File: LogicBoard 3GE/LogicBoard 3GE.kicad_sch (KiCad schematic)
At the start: 162 parts, among them IC201 2363, IC202 74LS00, IC203 74LS32, IC204 2114, IC205 2114, IC206 68A09, IC207 6522, IC208 AY3-8912, IC301 MC1408, IC302 CD4052B, IC303 LF347, IC304 LF353, IC305 4066, J201 CART, J202 DB9_Male, J203 DB9_Male, J204 Power, J301 Video, J302 Audio, Q301 2N3906, Q302 2N3906, Q303 2N3904, SW201 Reset, Y201 6MHz

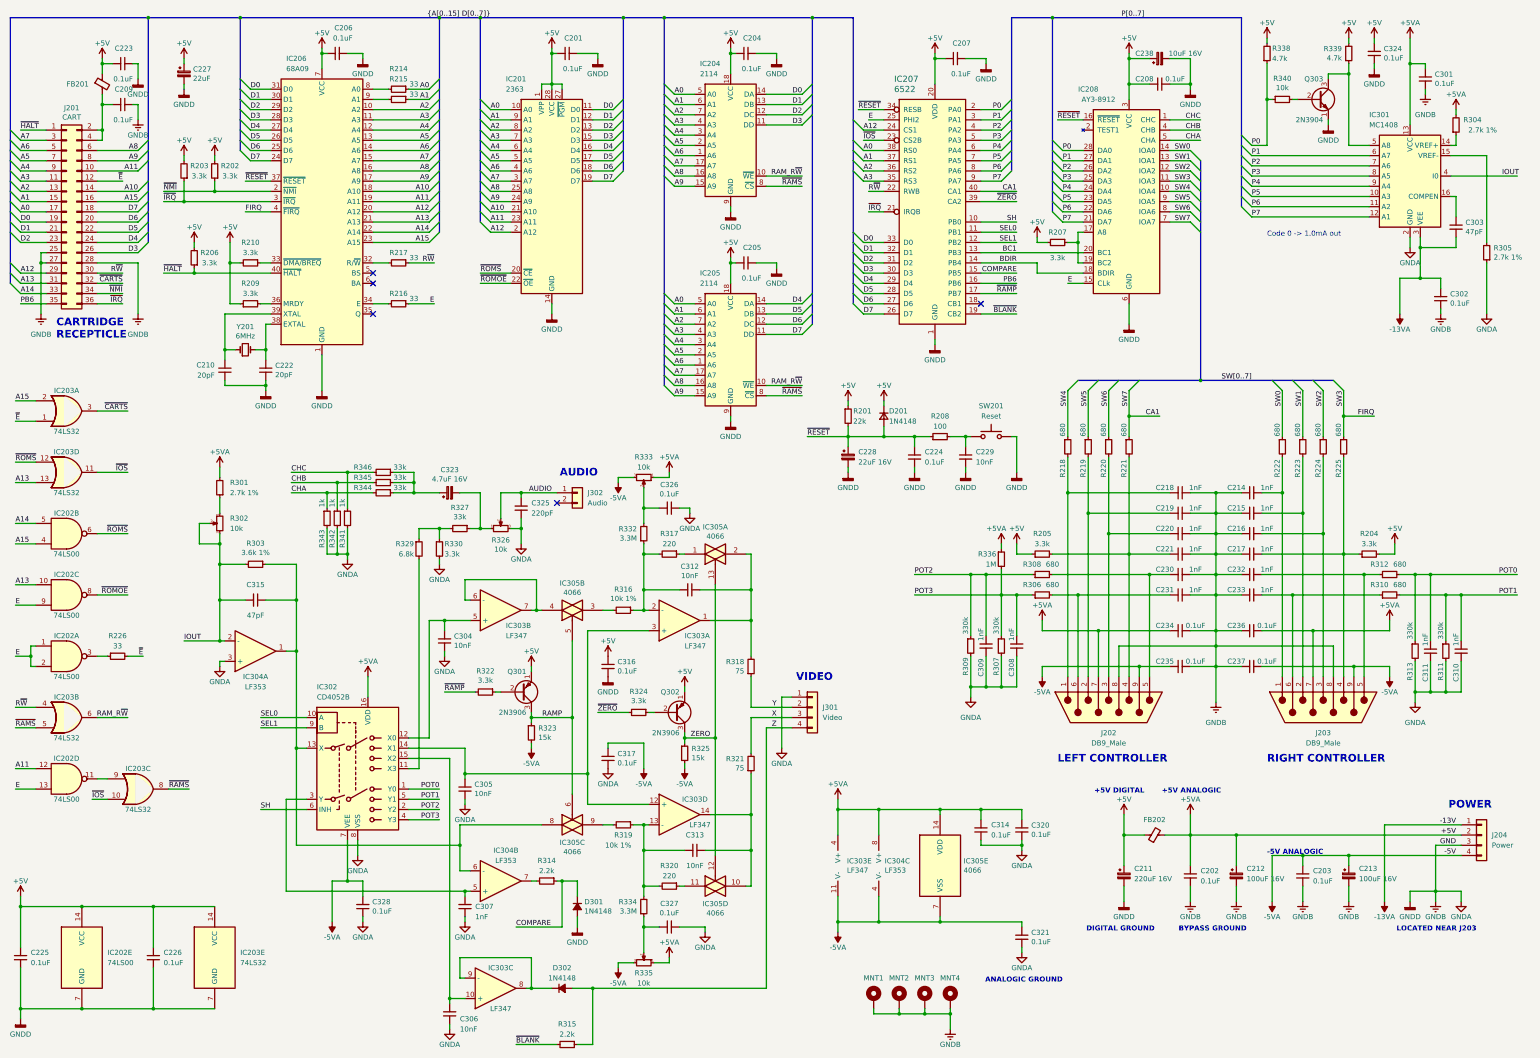
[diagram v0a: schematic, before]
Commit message: Correct inversion on IC301 bus
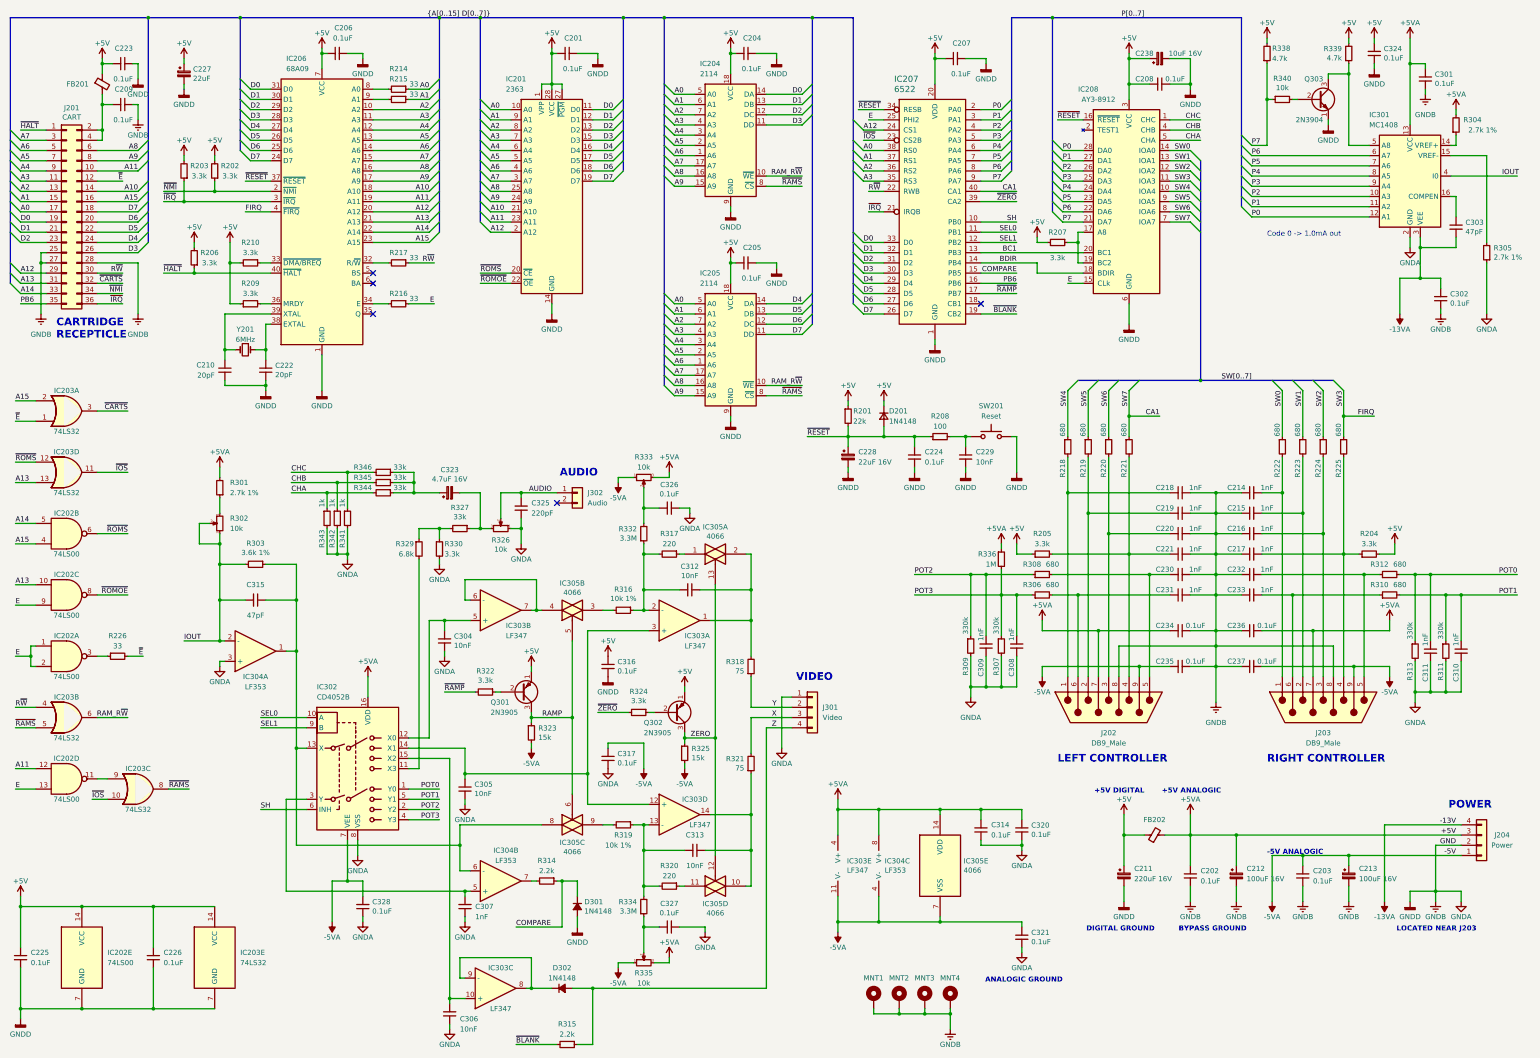
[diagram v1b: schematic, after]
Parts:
- removed Q301: 2N3906, Package_TO_SOT_THT:TO-92L_Wide, symbol Transistor_BJT:2N3906
- removed Q302: 2N3906, Package_TO_SOT_THT:TO-92_Wide, symbol Transistor_BJT:2N3906
- added Q301, Q302: 2N3905, Package_TO_SOT_THT:TO-92_Wide, symbol Transistor_BJT:2N3905
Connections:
- net +5V: now also J204.3 (Pin_3), R333.3, R335.3, Q301.1 (E), Q302.1 (E); no longer J204.2 (Pin_2), R333.1, R335.1
- net -12VA: now also J204.4 (Pin_4); no longer J204.1 (Pin_1)
- net -5VA: now also J204.1 (Pin_1), R333.1, R335.1; no longer J204.4 (Pin_4), R333.3, R335.3
- net GNDA: now also J204.2 (Pin_2), R326.1; no longer J204.3 (Pin_3), R326.3
- net P0: now also IC301.12 (A1); no longer R338.1, R340.1
- net P1: now also IC301.11 (A2); no longer IC301.6 (A7)
- net P2: now also IC301.10 (A3); no longer IC301.7 (A6)
- net P3: now also IC301.9 (A4); no longer IC301.8 (A5)
- net P4: now also IC301.8 (A5); no longer IC301.9 (A4)
- net P5: now also IC301.7 (A6); no longer IC301.10 (A3)
- net P6: now also IC301.6 (A7); no longer IC301.11 (A2)
- net P7: now also R338.1, R340.1; no longer IC301.12 (A1)
- net RAMP: now also Q301.3 (C)
- net ZERO: now also Q302.3 (C)
- net at R324.1: now also Q302.2 (B)
- net at C210.1, IC206.39 (XTAL): now also Y201.2; no longer Y201.1
- net at C222.1, IC206.38 (EXTAL): now also Y201.1; no longer Y201.2
- net at C323.2, R327.1: now also R326.3; no longer R326.1
- net at R322.1: now also Q301.2 (B)
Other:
- moved on the sheet: R326, R333, R335, Y201

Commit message: Add invisble label for BoardView
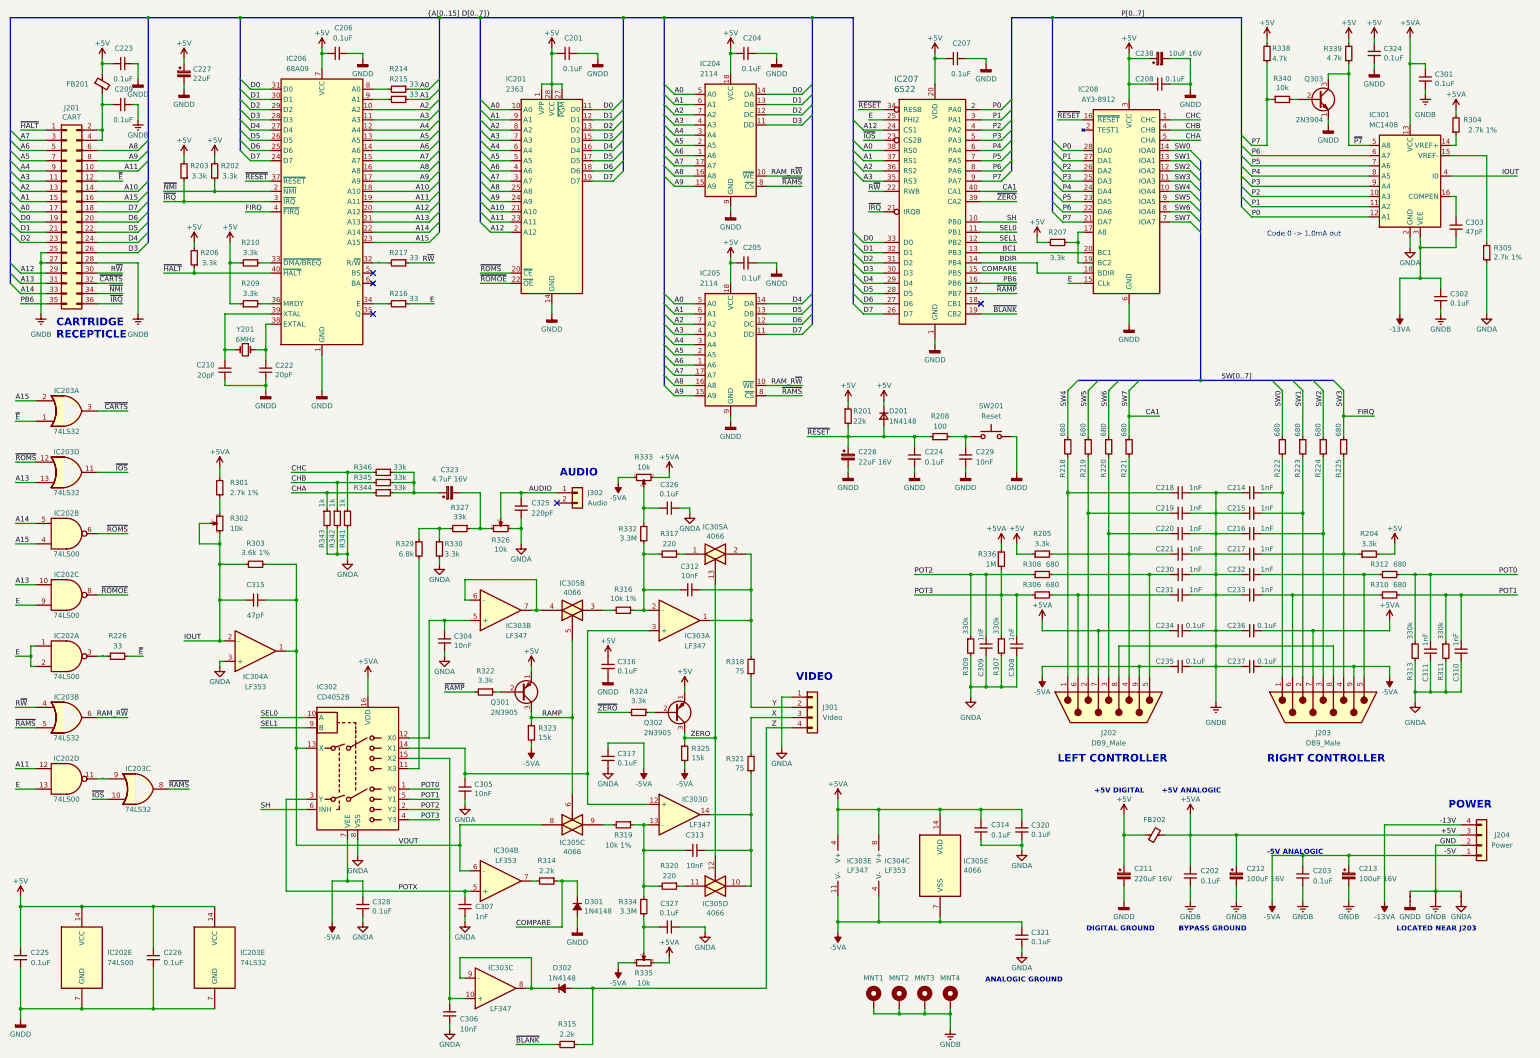
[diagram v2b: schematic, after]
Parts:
- added W1, W2, W3: W, symbol Vectrex LogicBoard:W
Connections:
- net GNDA: now also W3.1; no longer C201.2, C202.2, C203.2, C204.2, C205.2, C206.2, C207.2, C208.1, C209.2, C210.2, C211.2, C212.2, C213.2, C214.1, C215.1, C216.1, C217.1, C218.2, C219.2, C220.2, C221.2, C222.2, C223.2, C224.2, C225.2, C226.2, C227.2, C228.2, C229.2, C230.2, C231.2, C232.1, C233.1, C234.2, C235.2, C236.1, C237.1, C238.2, C301.1, C302.1, C316.1, C324.1, D301.2 (A), IC201.14 (GND), IC202.7 (GND), IC203.7 (GND), IC204.9 (GND), IC205.9 (GND), IC206.1 (GND), IC207.1 (GND), IC208.6 (GND), J201.25 (Pin_25), J201.27 (Pin_27), J201.28 (Pin_28), J202.8, J203.8, J204.2 (Pin_2), MNT1.1, MNT2.1, MNT3.1, MNT4.1, Q303.1 (E), SW201.2
- net J202_X: now reaches C230.1, J202.5, R308.2
- net IC303A_FB: now reaches C312.2, IC303.2 (-), R316.1, R317.2, R332.1
- net Y_OFFSET: now reaches C326.2, R332.2, R333.2
- net POTX: now reaches C307.2, IC302.3 (Y), IC304.5 (+)
- net EXTAL: now reaches C222.1, IC206.38 (EXTAL), Y201.1
- net XTAL: now reaches C210.1, IC206.39 (XTAL), Y201.2
- net J203_B2: now reaches C215.2, J203.2, R223.2
- net J202_B1: now reaches C218.1, J202.1, R218.2
- net J202_B2: now reaches C219.1, J202.2, R219.2
- net CH(A+B+C): now reaches C323.1, R344.1, R345.1, R346.1
- net J203_B1: now reaches C214.2, J203.1, R222.2
- net J203_B3: now reaches C216.2, J203.3, R224.2
- net J203_B4: now reaches C217.2, J203.4, R204.1, R225.2
- net J203_X: now reaches C232.2, J203.5, R312.1
- net J203_Y: now reaches C233.2, J203.6, R310.1
- net BC2: now reaches IC208.17 (A8), IC208.19 (BC2), R207.1
- net ~{A11&E}: now reaches IC202.11, IC203.9
- net SWITCH_RESET: now reaches C229.1, R208.2, SW201.1
- net Q301_BASE: now reaches Q301.2 (B), R322.1
- net CH(A+B+C)+DIGITAL_AUDIO: now reaches C323.2, R326.3, R327.1
- net IC303D_X: now reaches C313.1, IC303.14, IC305.10, R321.1
- net IC303D_FB: now reaches C313.2, IC303.13 (-), R319.1, R320.2, R334.2
- net Q302_BASE: now reaches Q302.2 (B), R324.1
- net VREF-: now reaches IC301.15 (VREF-), R305.2
- net VREF+: now reaches IC301.14 (VREF+), R304.1
- net COMPEN: now reaches C303.2, IC301.16 (COMPEN)
- net ~{P7}: now reaches IC301.5 (A8), Q303.3 (C), R339.1
- net X0: now reaches C304.1, IC302.12 (X0), IC303.5 (+)
- net CPU_A0: now reaches IC206.8 (A0), R214.2
- net X2: now reaches C306.2, IC302.15 (X2), IC303.10 (+)
- net IC202A_~{E}: now reaches IC202.3, R226.1
- net IC303C_FB: now reaches D302.1 (k), IC303.8, IC303.9 (-)
- net IC303A_Y: now reaches C312.1, IC303.1, IC305.2, R318.2
- net Q303_BASE: now reaches Q303.2 (B), R340.2
- net DIGITAL_AUDIO: now reaches R327.2, R329.1, R330.1
- net X3: now reaches IC302.11 (X3), R329.2
- net J202_Y: now reaches C231.1, J202.6, R306.2
- net J202_B3: now reaches C220.1, J202.3, R220.2
- net J202_B4: now reaches C221.1, J202.4, R205.2, R221.2
- net +5V_CART: now reaches C209.1, FB201.2, J201.2 (Pin_2), J201.4 (Pin_4)
- net X1: now reaches C305.2, IC302.14 (X1), IC303.12 (+), IC303.3 (+)
- net IC303B_FB: now reaches IC303.6 (-), IC303.7, IC305.4
- net CPU_R~{W}: now reaches IC206.32 (R/~{W}), R217.2
- net VOUT: now reaches C315.1, IC302.13 (X), IC304.1, IC304.6 (-), IC305.8, R303.1
- net CPU_E: now reaches IC206.34 (E), R216.2
- net CPU_A1: now reaches IC206.9 (A1), R215.2
- net X_OFFSET: now reaches C327.2, R334.1, R335.2
- new net GND: J204.2 (Pin_2), W1.2, W2.2, W3.2
- new net GNDD: C201.2, C204.2, C205.2, C206.2, C207.2, C208.1, C210.2, C211.2, C222.2, C223.2, C224.2, C225.2, C226.2, C227.2, C228.2, C229.2, C238.2, C316.1, C324.1, D301.2 (A), IC201.14 (GND), IC202.7 (GND), IC203.7 (GND), IC204.9 (GND), IC205.9 (GND), IC206.1 (GND), IC207.1 (GND), IC208.6 (GND), Q303.1 (E), SW201.2, W1.1
- new net GNDREF: C202.2, C203.2, C209.2, C212.2, C213.2, C214.1, C215.1, C216.1, C217.1, C218.2, C219.2, C220.2, C221.2, C230.2, C231.2, C232.1, C233.1, C234.2, C235.2, C236.1, C237.1, C301.1, C302.1, J201.25 (Pin_25), J201.27 (Pin_27), J201.28 (Pin_28), J202.8, J203.8, MNT1.1, MNT2.1, MNT3.1, MNT4.1, W2.1

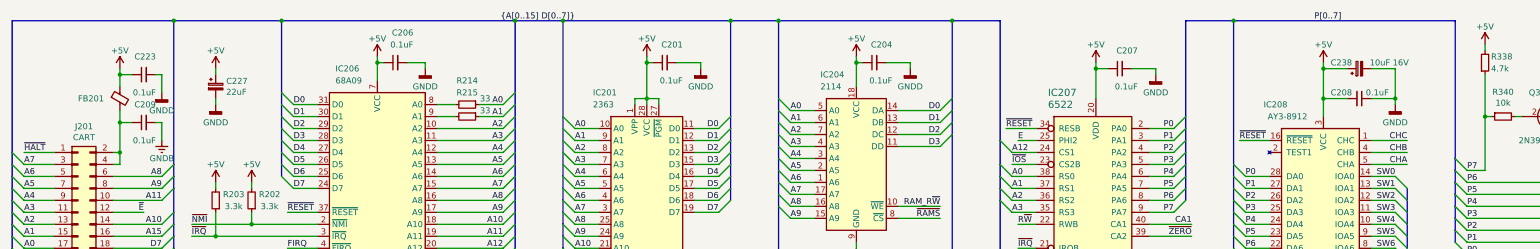
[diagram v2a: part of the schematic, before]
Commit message: Added a comment about the 9V voltage which is not 9V...
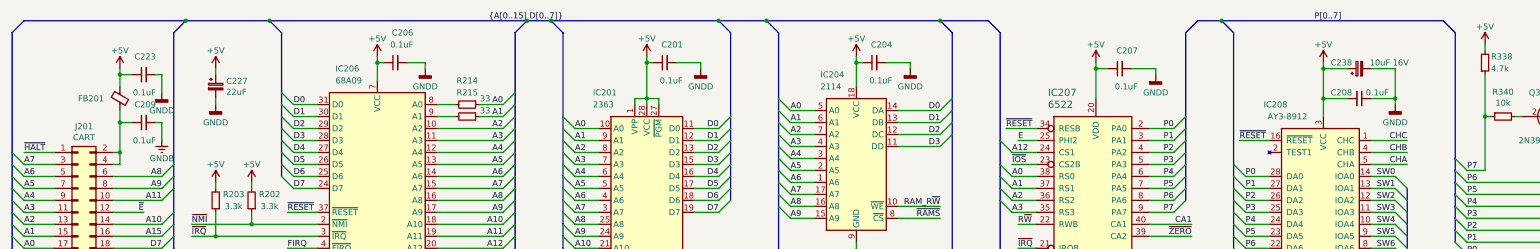
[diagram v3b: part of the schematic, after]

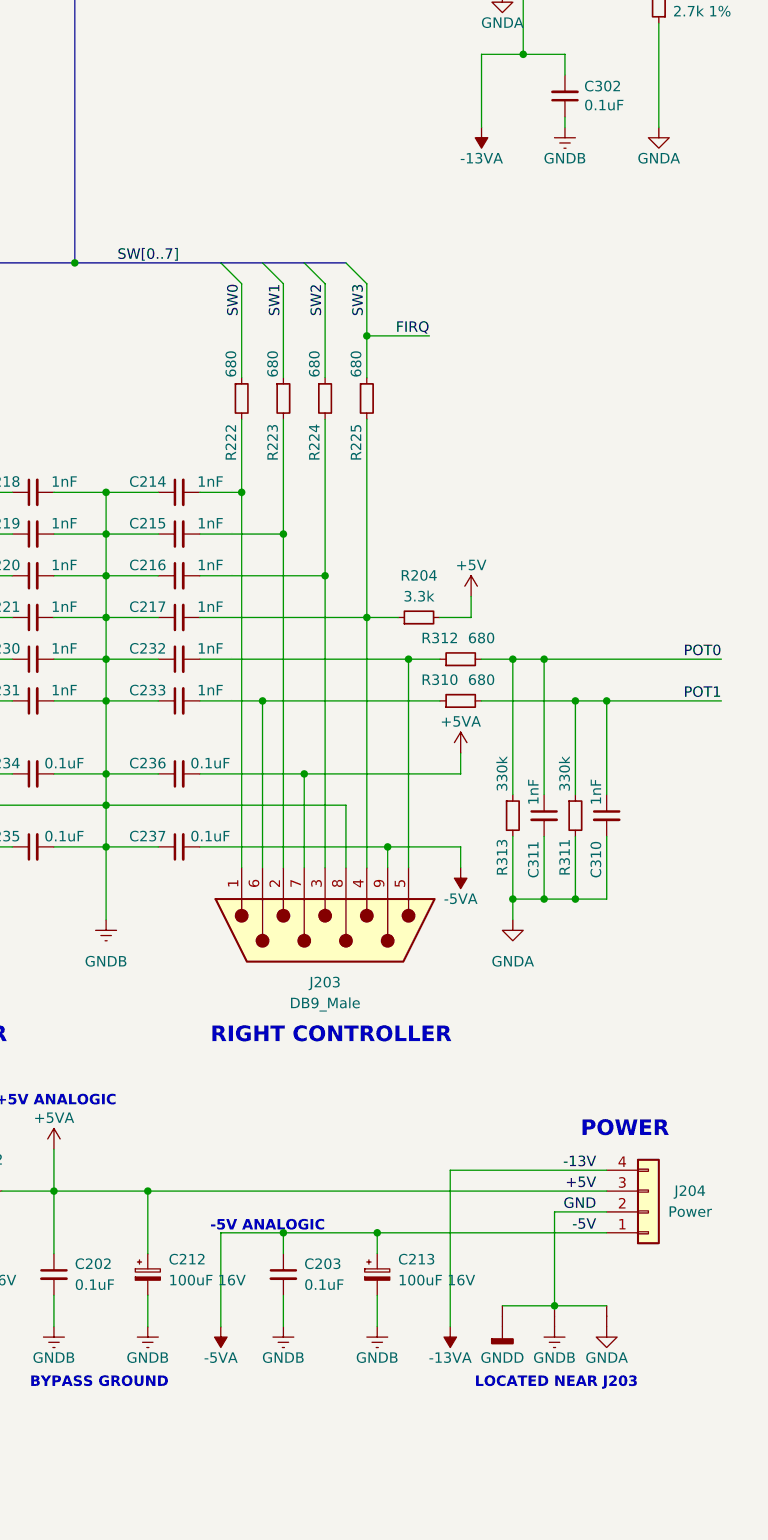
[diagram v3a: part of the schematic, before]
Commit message: Rename -13V to -13VREF
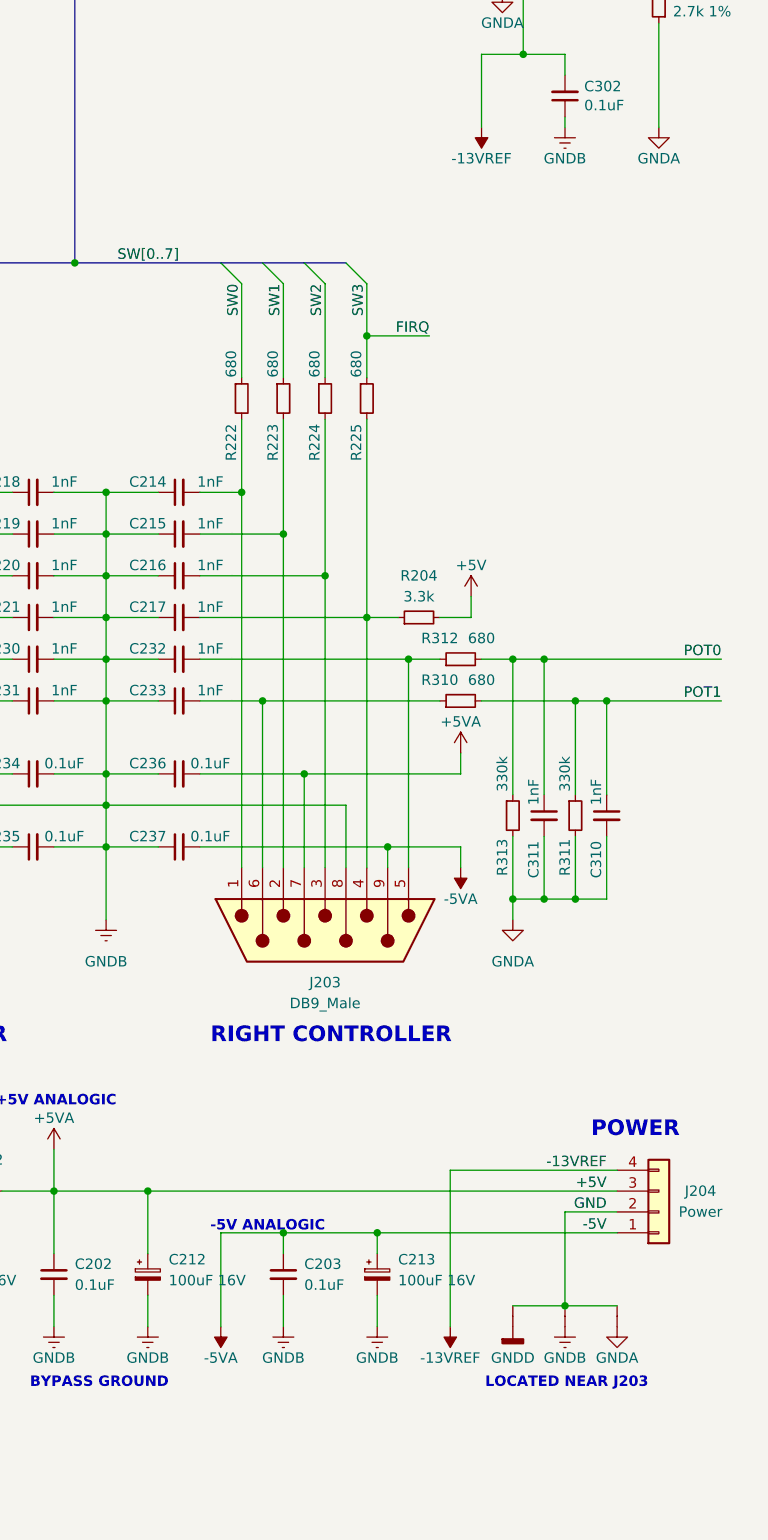
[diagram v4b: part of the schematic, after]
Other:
- moved on the sheet: J204
